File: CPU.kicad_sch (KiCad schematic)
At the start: 1 part

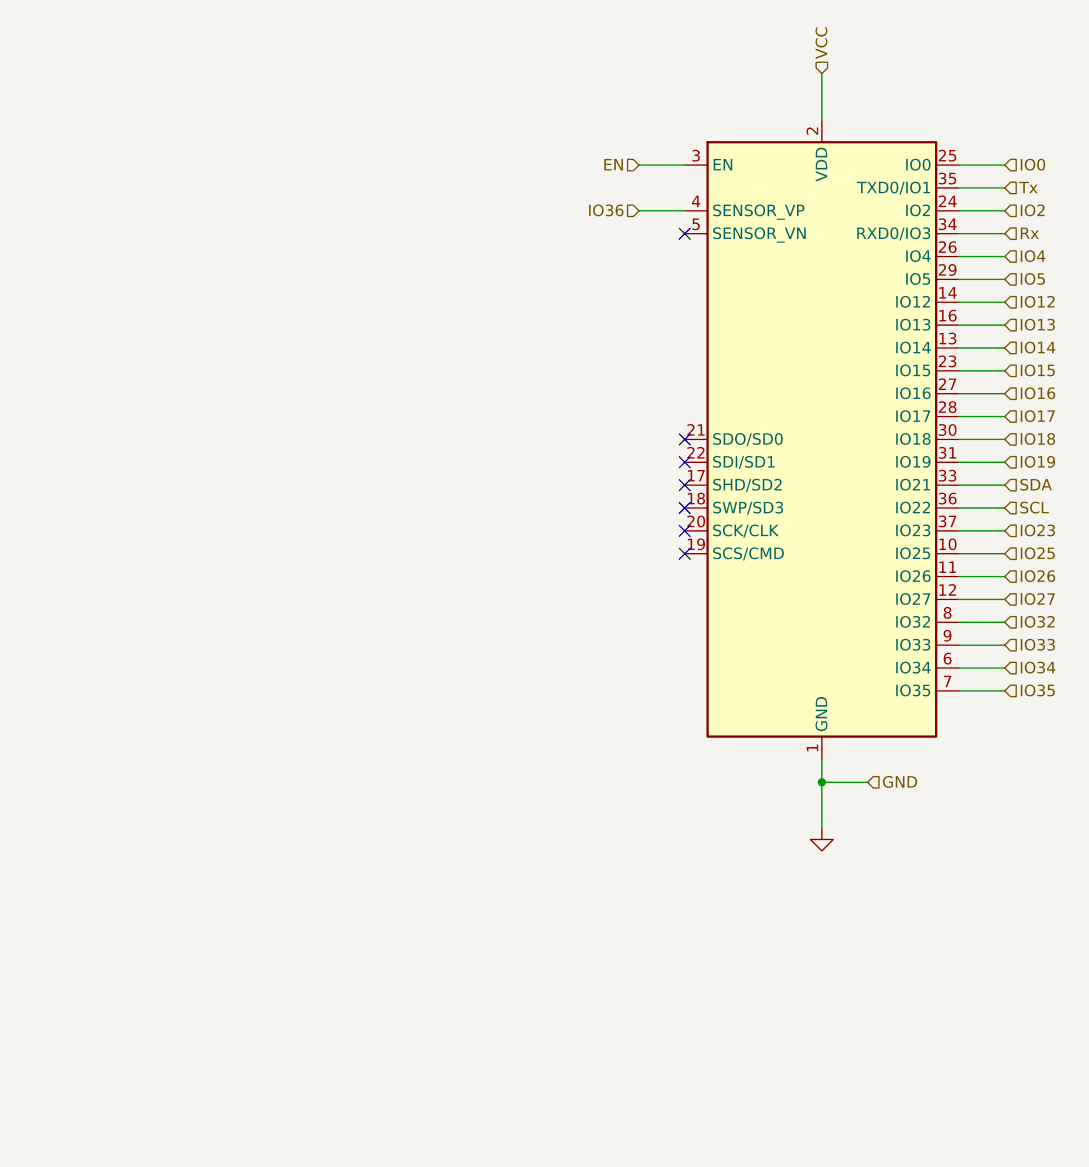
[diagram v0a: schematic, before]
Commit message: add entradas separadas
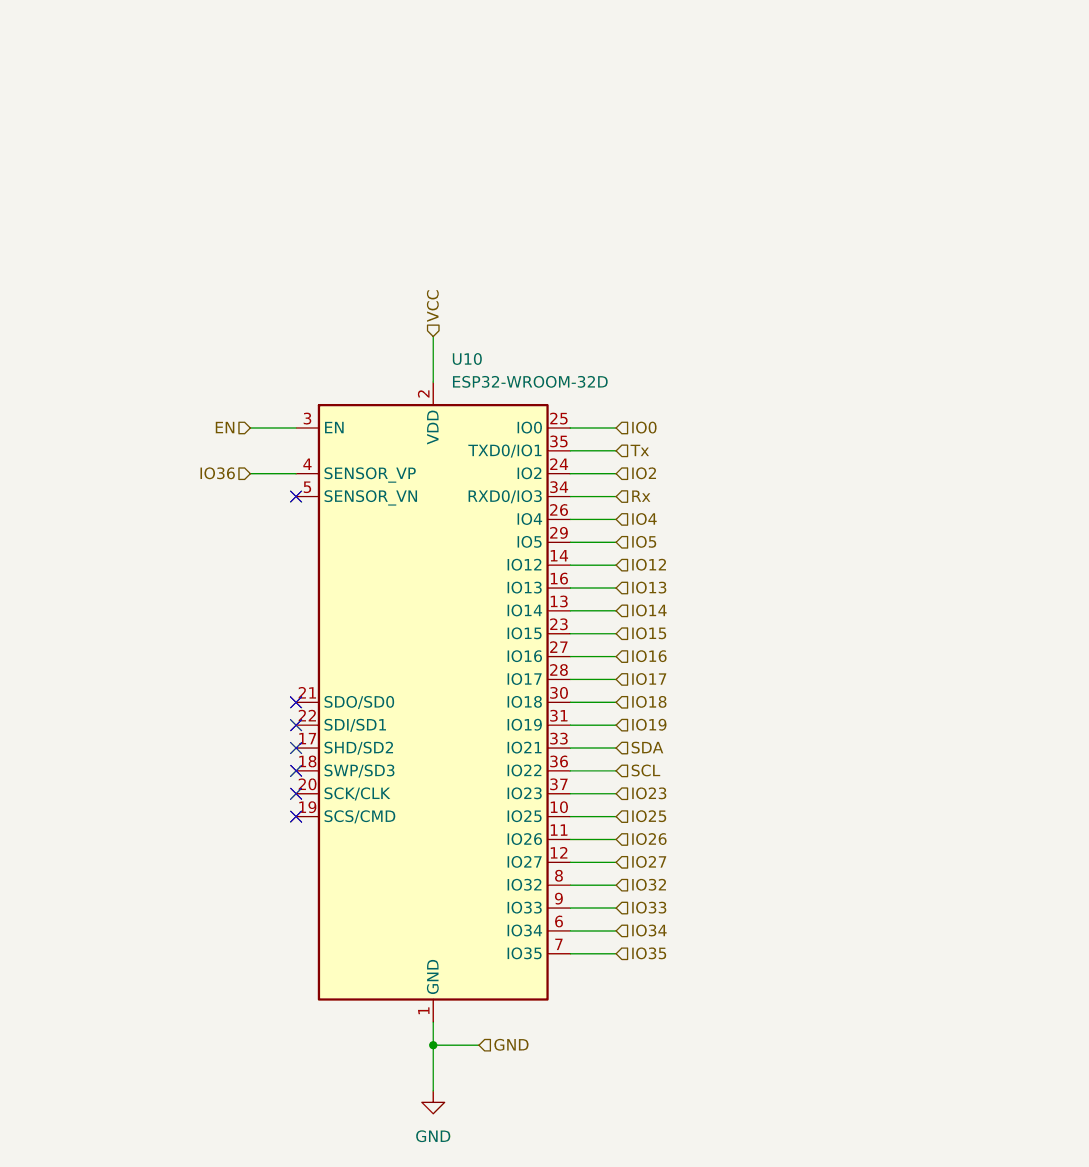
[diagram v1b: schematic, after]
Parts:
- U10: renamed from ?; value (none) -> ESP32-WROOM-32D; footprint (none) -> RF_Module:ESP32-WROOM-32

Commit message: input/output separadas
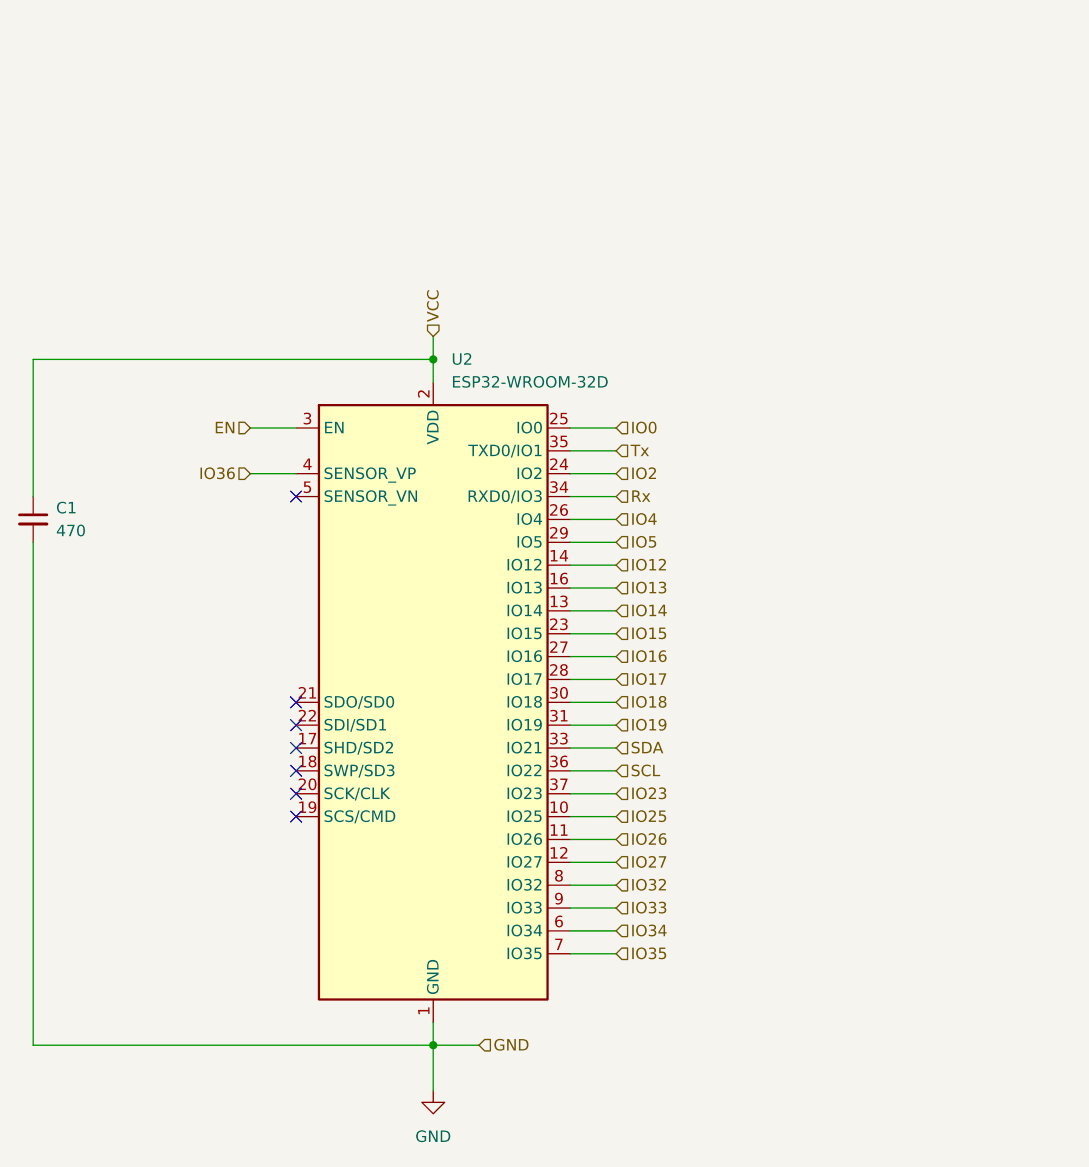
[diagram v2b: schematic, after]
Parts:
- added C1: 470, Capacitor_SMD:C_Elec_10x10.2, symbol Device:C_Small
- renumbered U10 to U2
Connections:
- net GND: now also C1.2
- net VCC: now also C1.1
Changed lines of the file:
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@@
   (title_block
     (title "CPU - ESP32")
-    (date "2022-09-15")
+    (date "2022-10-09")
     (rev "José Luis Laica")
     (company "INTEAMBI")
+  )
+  (junction (at 101.6 88.9) (diameter 0) (color 0 0 0 0)
   )
   (junction (at 101.6 165.1) (diameter 0) (color 0 0 0 0)
@@
     (stroke (width 0) (type default))
   )
-  (wire (pts (xy 101.6 86.36) (xy 101.6 91.44))
+  (wire (pts (xy 101.6 88.9) (xy 101.6 91.44))
+    (stroke (width 0) (type default))
+  )
+  (wire (pts (xy 101.6 86.36) (xy 101.6 88.9))
     (stroke (width 0) (type default))
   )
@@
     (stroke (width 0) (type default))
   )
+  (wire (pts (xy 57.15 88.9) (xy 101.6 88.9))
+    (stroke (width 0) (type default))
+  )
   (wire (pts (xy 121.92 129.54) (xy 116.84 129.54))
     (stroke (width 0) (type default))
@@
     (stroke (width 0) (type default))
   )
+  (wire (pts (xy 57.15 165.1) (xy 101.6 165.1))
+    (stroke (width 0) (type default))
+  )
   (wire (pts (xy 121.92 111.76) (xy 116.84 111.76))
     (stroke (width 0) (type default))
@@
     (stroke (width 0) (type default))
   )
+  (wire (pts (xy 57.15 109.22) (xy 57.15 165.1))
+    (stroke (width 0) (type default))
+  )
   (wire (pts (xy 121.92 149.86) (xy 116.84 149.86))
+    (stroke (width 0) (type default))
+  )
+  (wire (pts (xy 57.15 104.14) (xy 57.15 88.9))
     (stroke (width 0) (type default))
   )
@@
   (symbol (lib_id "power:GND") (at 101.6 170.18 0) (unit 1)
     (in_bom yes) (on_board yes) (dnp no) (fields_autoplaced)
-    (property "Reference" "#PWR031" (at 101.6 176.53 0)
+    (property "Reference" "#PWR04" (at 101.6 176.53 0)
       (effects (font (size 1.27 1.27)) hide)
     )
@@
       (project "PLC 32 V2"
         (path "/d17a54f1-6eda-453f-95e1-42a53b02a1c3/75bbcb0a-0b0c-4eec-8c3a-7589e42d8fef"
-          (reference "#PWR031") (unit 1) (value "GND") (footprint "")
+          (reference "#PWR04") (unit 1) (value "GND") (footprint "")
         )
       )
     )
   )
+  (symbol (lib_id "Device:C_Small") (at 57.15 106.68 0) (unit 1)
+    (in_bom yes) (on_board yes) (dnp no) (fields_autoplaced)
+    (property "Reference" "C1" (at 59.69 105.4162 0)
+      (effects (font (size 1.27 1.27)) (justify left))
+    )
+    (property "Value" "470" (at 59.69 107.9562 0)
+      (effects (font (size 1.27 1.27)) (justify left))
+    )
+    (property "Footprint" "Capacitor_SMD:C_Elec_10x10.2" (at 57.15 106.68 0)
+      (effects (font (size 1.27 1.27)) hide)
+    )
+    (property "Datasheet" "~" (at 57.15 106.68 0)
+      (effects (font (size 1.27 1.27)) hide)
+    )
+    (pin "1")
+    (pin "2")
+    (instances
+      (project "PLC 32 V2"
+        (path "/d17a54f1-6eda-453f-95e1-42a53b02a1c3/4477056d-8edb-4f95-828f-5c12bb786be6"
+          (reference "C1") (unit 1) (value "470") (footprint "Capacitor_SMD:C_Elec_10x10.2")
+        )
+        (path "/d17a54f1-6eda-453f-95e1-42a53b02a1c3/75bbcb0a-0b0c-4eec-8c3a-7589e42d8fef"
+          (reference "C3") (unit 1) (value "470") (footprint "Capacitor_SMD:C_Elec_10x10.2")
+        )
+      )
+    )
+  )
   (symbol (lib_id "RF_Module:ESP32-WROOM-32D") (at 101.6 127 0) (unit 1)
     (in_bom yes) (on_board yes) (dnp no) (fields_autoplaced)
-    (property "Reference" "U10" (at 103.6194 88.9 0)
+    (property "Reference" "U2" (at 103.6194 88.9 0)
       (effects (font (size 1.27 1.27)) (justify left))
     )
@@
       (project "PLC 32 V2"
         (path "/d17a54f1-6eda-453f-95e1-42a53b02a1c3/75bbcb0a-0b0c-4eec-8c3a-7589e42d8fef"
-          (reference "U10") (unit 1) (value "ESP32-WROOM-32D") (footprint "RF_Module:ESP32-WROOM-32")
+          (reference "U2") (unit 1) (value "ESP32-WROOM-32D") (footprint "RF_Module:ESP32-WROOM-32")
         )
       )

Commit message: add
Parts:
- U3: renamed from U2; footprint RF_Module:ESP32-WROOM-32 -> RF_Module:ESP32-WROOM-32U
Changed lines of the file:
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@@
     (stroke (width 0) (type default))
   )
-  (wire (pts (xy 101.6 86.36) (xy 101.6 88.9))
+  (wire (pts (xy 101.6 81.28) (xy 101.6 88.9))
     (stroke (width 0) (type default))
   )
@@
     (stroke (width 0) (type default))
   )
+  (wire (pts (xy 81.28 101.6) (xy 86.36 101.6))
+    (stroke (width 0) (type default))
+  )
   (wire (pts (xy 81.28 96.52) (xy 86.36 96.52))
     (stroke (width 0) (type default))
@@
   )
   (wire (pts (xy 121.92 144.78) (xy 116.84 144.78))
-    (stroke (width 0) (type default))
-  )
-  (wire (pts (xy 81.28 101.6) (xy 86.36 101.6))
     (stroke (width 0) (type default))
   )
@@
     (effects (font (size 1.27 1.27)) (justify left))
   )
-  (hierarchical_label "VCC" (shape input) (at 101.6 86.36 90) (fields_autoplaced)
+  (hierarchical_label "VCC" (shape output) (at 101.6 81.28 90) (fields_autoplaced)
     (effects (font (size 1.27 1.27)) (justify left))
   )
@@
         )
         (path "/d17a54f1-6eda-453f-95e1-42a53b02a1c3/75bbcb0a-0b0c-4eec-8c3a-7589e42d8fef"
-          (reference "C3") (unit 1) (value "470") (footprint "Capacitor_SMD:C_Elec_10x10.2")
+          (reference "C4") (unit 1) (value "470") (footprint "Capacitor_SMD:C_Elec_10x10.2")
         )
       )
@@
   (symbol (lib_id "RF_Module:ESP32-WROOM-32D") (at 101.6 127 0) (unit 1)
     (in_bom yes) (on_board yes) (dnp no) (fields_autoplaced)
-    (property "Reference" "U2" (at 103.6194 88.9 0)
+    (property "Reference" "U3" (at 103.6194 88.9 0)
       (effects (font (size 1.27 1.27)) (justify left))
     )
@@
       (effects (font (size 1.27 1.27)) (justify left))
     )
-    (property "Footprint" "RF_Module:ESP32-WROOM-32" (at 101.6 165.1 0)
+    (property "Footprint" "RF_Module:ESP32-WROOM-32U" (at 101.6 165.1 0)
       (effects (font (size 1.27 1.27)) hide)
     )
@@
       (project "PLC 32 V2"
         (path "/d17a54f1-6eda-453f-95e1-42a53b02a1c3/75bbcb0a-0b0c-4eec-8c3a-7589e42d8fef"
-          (reference "U2") (unit 1) (value "ESP32-WROOM-32D") (footprint "RF_Module:ESP32-WROOM-32")
+          (reference "U3") (unit 1) (value "ESP32-WROOM-32D") (footprint "RF_Module:ESP32-WROOM-32U")
         )
       )
